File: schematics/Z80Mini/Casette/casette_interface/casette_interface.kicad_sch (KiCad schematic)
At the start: 32 parts, among them J6 CASETTE/AUDIO, K1 ADW11, Q4 BC337

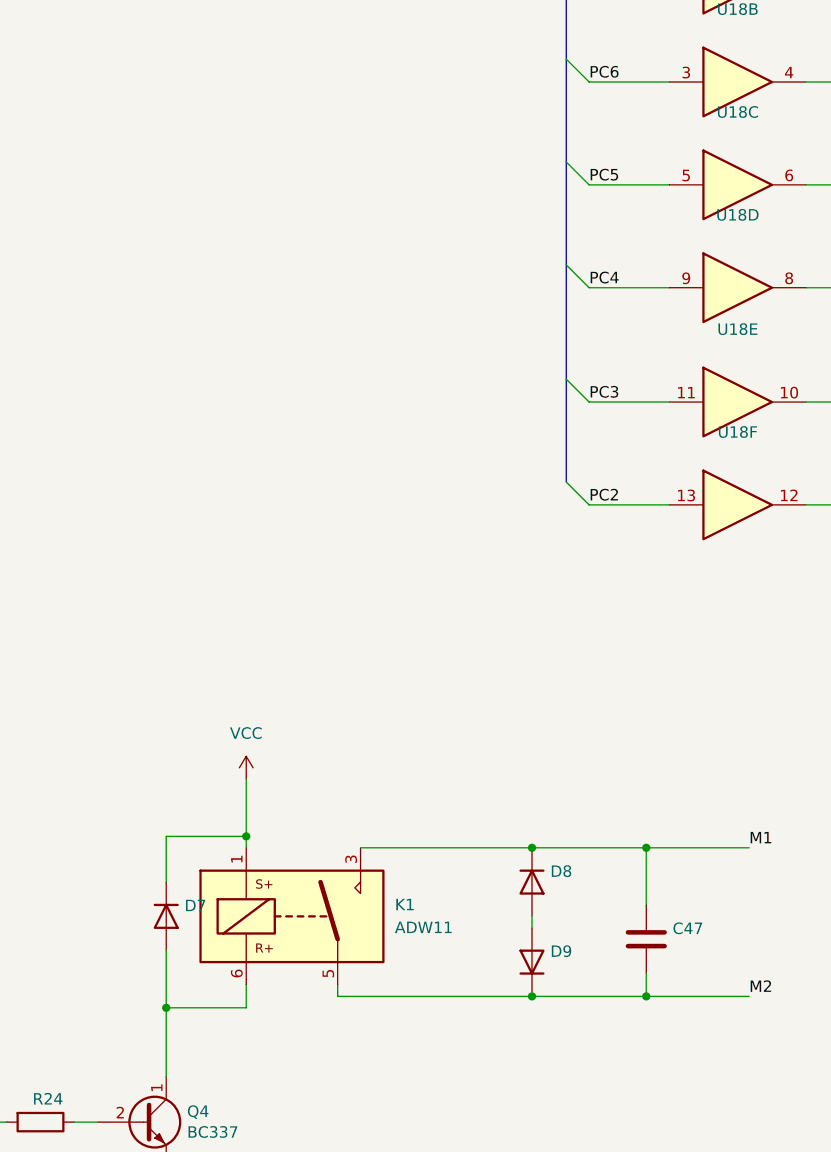
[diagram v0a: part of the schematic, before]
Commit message: Latest changes for adapt source to support Z80AllInOne adding some macros and latest schematic improvements
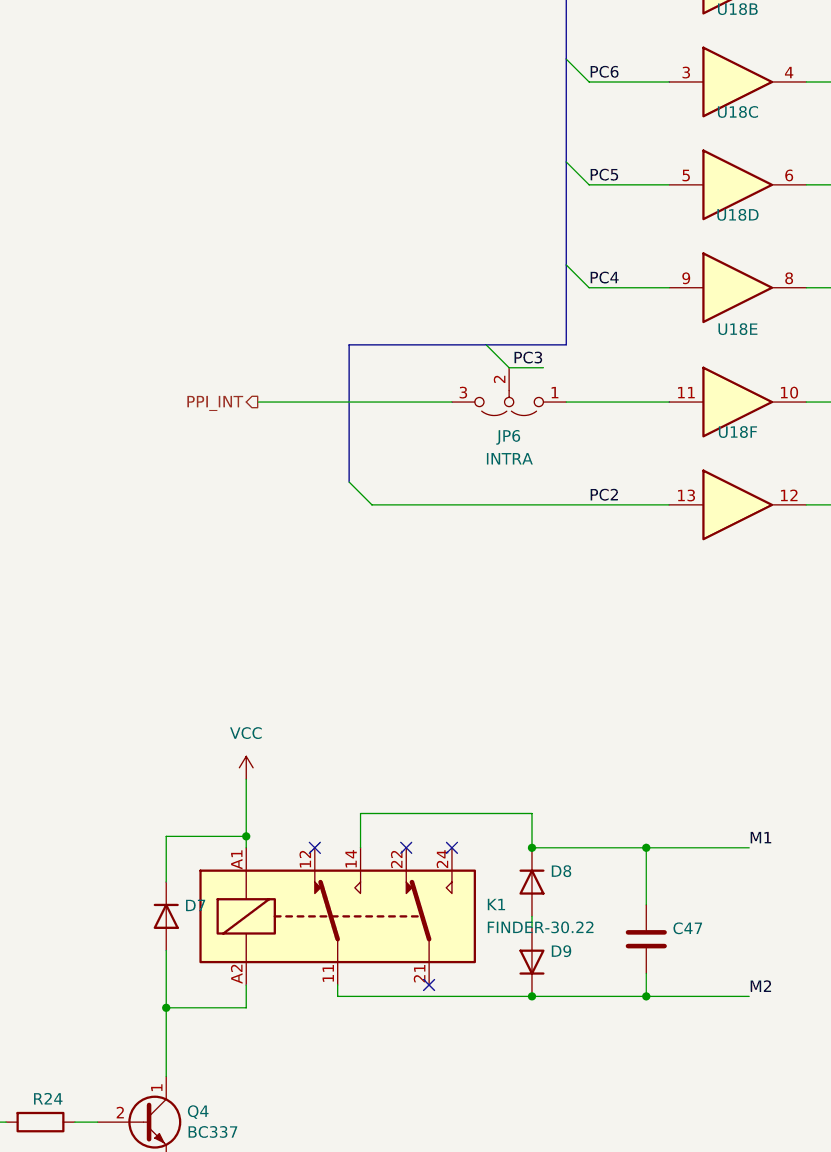
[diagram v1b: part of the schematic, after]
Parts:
- removed K1: ADW11, Relay_THT:Relay_1P1T_NO_10x24x18.8mm_Panasonic_ADW11xxxxW_THT, symbol Relay:ADW11
- added JP6: INTRA, Connector_PinHeader_2.54mm:PinHeader_1x03_P2.54mm_Vertical, symbol Jumper:Jumper_3_Open
- added K1: FINDER-30.22, Relay_THT:Relay_DPDT_Finder_30.22, symbol Relay:FINDER-30.22
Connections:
- net M1: now also K1.14
- net M2: now also K1.11
- net PC3: now also JP6.2 (C); no longer U18.11
- net VCC: now also K1.A1
- net at D7.1 (A), Q4.1 (C): now also K1.A2
- new net: JP6.1 (A), U18.11
- new net PPI_INT: JP6.3 (B)
- no-connect marks 0 -> 4
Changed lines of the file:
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@@
   (junction (at 242.57 144.78) (diameter 0) (color 0 0 0 0)
   )
+  (junction (at 44.45 151.13) (diameter 0) (color 0 0 0 0)
+  )
+  (junction (at 149.86 95.25) (diameter 0) (color 0 0 0 0)
+  )
+  (junction (at 134.62 48.26) (diameter 0) (color 0 0 0 0)
+  )
+  (junction (at 134.62 36.83) (diameter 0) (color 0 0 0 0)
+  )
+  (junction (at 97.79 133.35) (diameter 0) (color 0 0 0 0)
+  )
+  (junction (at 229.87 144.78) (diameter 0) (color 0 0 0 0)
+  )
   (junction (at 85.09 133.35) (diameter 0) (color 0 0 0 0)
   )
-  (junction (at 44.45 151.13) (diameter 0) (color 0 0 0 0)
-  )
-  (junction (at 149.86 95.25) (diameter 0) (color 0 0 0 0)
-  )
-  (junction (at 134.62 48.26) (diameter 0) (color 0 0 0 0)
-  )
-  (junction (at 134.62 36.83) (diameter 0) (color 0 0 0 0)
-  )
-  (junction (at 97.79 133.35) (diameter 0) (color 0 0 0 0)
-  )
-  (junction (at 229.87 144.78) (diameter 0) (color 0 0 0 0)
-  )
   (junction (at 167.64 129.54) (diameter 0) (color 0 0 0 0)
   )
@@
   (junction (at 134.62 71.12) (diameter 0) (color 0 0 0 0)
   )
+  (no_connect (at 60.96 133.35))
+  (no_connect (at 73.66 148.59))
+  (no_connect (at 71.12 133.35))
+  (no_connect (at 76.2 133.35))
   (bus_entry (at 88.9 68.58) (size 2.54 2.54)
     (stroke (width 0) (type default) (color 0 0 0 0))
   )
-  (bus_entry (at 88.9 81.28) (size 2.54 2.54)
-    (stroke (width 0) (type default) (color 0 0 0 0))
-  )
-  (bus_entry (at 88.9 92.71) (size 2.54 2.54)
+  (bus_entry (at 64.77 92.71) (size 2.54 2.54)
     (stroke (width 0) (type default) (color 0 0 0 0))
   )
@@
     (stroke (width 0) (type default) (color 0 0 0 0))
   )
+  (bus_entry (at 80.01 77.47) (size 2.54 2.54)
+    (stroke (width 0) (type default) (color 0 0 0 0))
+  )
   (wire (pts (xy 151.13 45.72) (xy 165.1 45.72))
     (stroke (width 0) (type default) (color 0 0 0 0))
   )
+  (wire (pts (xy 66.04 133.35) (xy 66.04 129.54))
+    (stroke (width 0) (type default) (color 0 0 0 0))
+  )
   (wire (pts (xy 63.5 149.86) (xy 85.09 149.86))
     (stroke (width 0) (type default) (color 0 0 0 0))
@@
     (stroke (width 0) (type default) (color 0 0 0 0))
   )
-  (wire (pts (xy 66.04 133.35) (xy 85.09 133.35))
-    (stroke (width 0) (type default) (color 0 0 0 0))
-  )
   (wire (pts (xy 44.45 144.78) (xy 44.45 151.13))
     (stroke (width 0) (type default) (color 0 0 0 0))
@@
     (stroke (width 0) (type default) (color 0 0 0 0))
   )
+  (bus (pts (xy 88.9 68.58) (xy 88.9 57.15))
+    (stroke (width 0) (type default) (color 0 0 0 0))
+  )
   (wire (pts (xy 185.42 144.78) (xy 199.39 144.78))
     (stroke (width 0) (type default) (color 0 0 0 0))
@@
     (stroke (width 0) (type default) (color 0 0 0 0))
   )
-  (bus (pts (xy 88.9 57.15) (xy 88.9 68.58))
+  (wire (pts (xy 54.61 83.82) (xy 76.2 83.82))
     (stroke (width 0) (type default) (color 0 0 0 0))
   )
@@
     (stroke (width 0) (type default) (color 0 0 0 0))
   )
+  (bus (pts (xy 88.9 68.58) (xy 88.9 77.47))
+    (stroke (width 0) (type default) (color 0 0 0 0))
+  )
   (wire (pts (xy 85.09 140.97) (xy 85.09 142.24))
     (stroke (width 0) (type default) (color 0 0 0 0))
@@
     (stroke (width 0) (type default) (color 0 0 0 0))
   )
+  (wire (pts (xy 66.04 129.54) (xy 85.09 129.54))
+    (stroke (width 0) (type default) (color 0 0 0 0))
+  )
   (wire (pts (xy 100.33 71.12) (xy 91.44 71.12))
     (stroke (width 0) (type default) (color 0 0 0 0))
@@
     (stroke (width 0) (type default) (color 0 0 0 0))
   )
+  (wire (pts (xy 85.09 129.54) (xy 85.09 133.35))
+    (stroke (width 0) (type default) (color 0 0 0 0))
+  )
   (wire (pts (xy 128.27 36.83) (xy 134.62 36.83))
     (stroke (width 0) (type default) (color 0 0 0 0))
@@
     (stroke (width 0) (type default) (color 0 0 0 0))
   )
-  (bus (pts (xy 88.9 68.58) (xy 88.9 81.28))
-    (stroke (width 0) (type default) (color 0 0 0 0))
-  )
   (wire (pts (xy 115.57 48.26) (xy 120.65 48.26))
     (stroke (width 0) (type default) (color 0 0 0 0))
@@
     (stroke (width 0) (type default) (color 0 0 0 0))
   )
+  (bus (pts (xy 88.9 77.47) (xy 80.01 77.47))
+    (stroke (width 0) (type default) (color 0 0 0 0))
+  )
   (wire (pts (xy 170.18 142.24) (xy 167.64 142.24))
     (stroke (width 0) (type default) (color 0 0 0 0))
@@
     (stroke (width 0) (type default) (color 0 0 0 0))
   )
+  (bus (pts (xy 64.77 77.47) (xy 64.77 92.71))
+    (stroke (width 0) (type default) (color 0 0 0 0))
+  )
   (wire (pts (xy 242.57 154.94) (xy 242.57 160.02))
     (stroke (width 0) (type default) (color 0 0 0 0))
@@
     (stroke (width 0) (type default) (color 0 0 0 0))
   )
-  (wire (pts (xy 100.33 95.25) (xy 91.44 95.25))
+  (wire (pts (xy 100.33 95.25) (xy 67.31 95.25))
     (stroke (width 0) (type default) (color 0 0 0 0))
   )
@@
     (stroke (width 0) (type default) (color 0 0 0 0))
   )
-  (wire (pts (xy 100.33 83.82) (xy 91.44 83.82))
+  (wire (pts (xy 100.33 83.82) (xy 88.9 83.82))
     (stroke (width 0) (type default) (color 0 0 0 0))
   )
@@
     (stroke (width 0) (type default) (color 0 0 0 0))
   )
-  (bus (pts (xy 88.9 81.28) (xy 88.9 92.71))
-    (stroke (width 0) (type default) (color 0 0 0 0))
-  )
   (wire (pts (xy 242.57 95.25) (xy 242.57 144.78))
     (stroke (width 0) (type default) (color 0 0 0 0))
@@
     (stroke (width 0) (type default) (color 0 0 0 0))
   )
+  (bus (pts (xy 80.01 77.47) (xy 64.77 77.47))
+    (stroke (width 0) (type default) (color 0 0 0 0))
+  )
   (wire (pts (xy 115.57 83.82) (xy 120.65 83.82))
     (stroke (width 0) (type default) (color 0 0 0 0))
@@
   )
   (wire (pts (xy 85.09 133.35) (xy 97.79 133.35))
+    (stroke (width 0) (type default) (color 0 0 0 0))
+  )
+  (wire (pts (xy 86.36 80.01) (xy 82.55 80.01))
     (stroke (width 0) (type default) (color 0 0 0 0))
   )
@@
     (effects (font (size 1.27 1.27)) (justify left bottom))
   )
+  (label "PC3" (at 86.36 80.01 180)
+    (effects (font (size 1.27 1.27)) (justify right bottom))
+  )
   (label "M2" (at 181.61 81.28 0)
     (effects (font (size 1.27 1.27)) (justify left bottom))
@@
     (effects (font (size 1.27 1.27)) (justify left bottom))
   )
-  (label "PC3" (at 91.44 83.82 0)
-    (effects (font (size 1.27 1.27)) (justify left bottom))
-  )
   (label "M2" (at 109.22 149.86 0)
     (effects (font (size 1.27 1.27)) (justify left bottom))
@@
   )
   (hierarchical_label "PA7" (shape input) (at 21.59 163.83 180)
+    (effects (font (size 1.27 1.27)) (justify right))
+  )
+  (hierarchical_label "PPI_INT" (shape output) (at 54.61 83.82 180)
     (effects (font (size 1.27 1.27)) (justify right))
   )
@@
     (pin "3")
   )
+  (symbol (lib_id "Relay:FINDER-30.22") (at 63.5 140.97 0) (unit 1)
+    (in_bom yes) (on_board yes) (fields_autoplaced)
+    (property "Reference" "K1" (id 0) (at 80.01 139.6999 0)
+      (effects (font (size 1.27 1.27)) (justify left))
+    )
+    (property "Value" "FINDER-30.22" (id 1) (at 80.01 142.2399 0)
+      (effects (font (size 1.27 1.27)) (justify left))
+    )
+    (property "Footprint" "Relay_THT:Relay_DPDT_Finder_30.22" (id 2) (at 97.79 141.732 0)
+      (effects (font (size 1.27 1.27)) hide)
+    )
+    (property "Datasheet" "http://gfinder.findernet.com/assets/Series/354/S30EN.pdf" (id 3) (at 63.5 140.97 0)
+      (effects (font (size 1.27 1.27)) hide)
+    )
+    (pin "11")
+    (pin "12")
+    (pin "14")
+    (pin "21")
+    (pin "22")
+    (pin "24")
+    (pin "A1")
+    (pin "A2")
+  )
   (symbol (lib_id "power:VCC") (at 50.8 26.67 0) (unit 1)
     (in_bom yes) (on_board yes)
@@
     )
     (pin "1")
-  )
-  (symbol (lib_id "Relay:ADW11") (at 58.42 140.97 0) (unit 1)
-    (in_bom yes) (on_board yes) (fields_autoplaced)
-    (property "Reference" "K1" (id 0) (at 69.85 139.6999 0)
-      (effects (font (size 1.27 1.27)) (justify left))
-    )
-    (property "Value" "ADW11" (id 1) (at 69.85 142.2399 0)
-      (effects (font (size 1.27 1.27)) (justify left))
-    )
-    (property "Footprint" "Relay_THT:Relay_1P1T_NO_10x24x18.8mm_Panasonic_ADW11xxxxW_THT" (id 2) (at 92.075 142.24 0)
-      (effects (font (size 1.27 1.27)) hide)
-    )
-    (property "Datasheet" "https://www.panasonic-electric-works.com/pew/es/downloads/ds_dw_hl_en.pdf" (id 3) (at 58.42 140.97 0)
-      (effects (font (size 1.27 1.27)) hide)
-    )
-    (pin "1")
-    (pin "3")
-    (pin "5")
-    (pin "6")
   )
   (symbol (lib_id "power:VCC") (at 199.39 116.84 0) (unit 1)
@@
     (pin "1")
   )
+  (symbol (lib_id "Jumper:Jumper_3_Open") (at 82.55 83.82 180) (unit 1)
+    (in_bom yes) (on_board yes) (fields_autoplaced)
+    (property "Reference" "JP6" (id 0) (at 82.55 87.63 0))
+    (property "Value" "INTRA" (id 1) (at 82.55 90.17 0))
+    (property "Footprint" "Connector_PinHeader_2.54mm:PinHeader_1x03_P2.54mm_Vertical" (id 2) (at 82.55 83.82 0)
+      (effects (font (size 1.27 1.27)) hide)
+    )
+    (property "Datasheet" "~" (id 3) (at 82.55 83.82 0)
+      (effects (font (size 1.27 1.27)) hide)
+    )
+    (pin "1")
+    (pin "2")
+    (pin "3")
+  )
   (symbol (lib_id "power:GND") (at 151.13 176.53 0) (unit 1)
